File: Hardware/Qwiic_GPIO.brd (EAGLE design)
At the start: 38.1 x 38.1 mm, 74 parts, among them J2 SMD, J3 PTH, J4 SMD, J7 455-1750-1-ND, U3 TCA9534

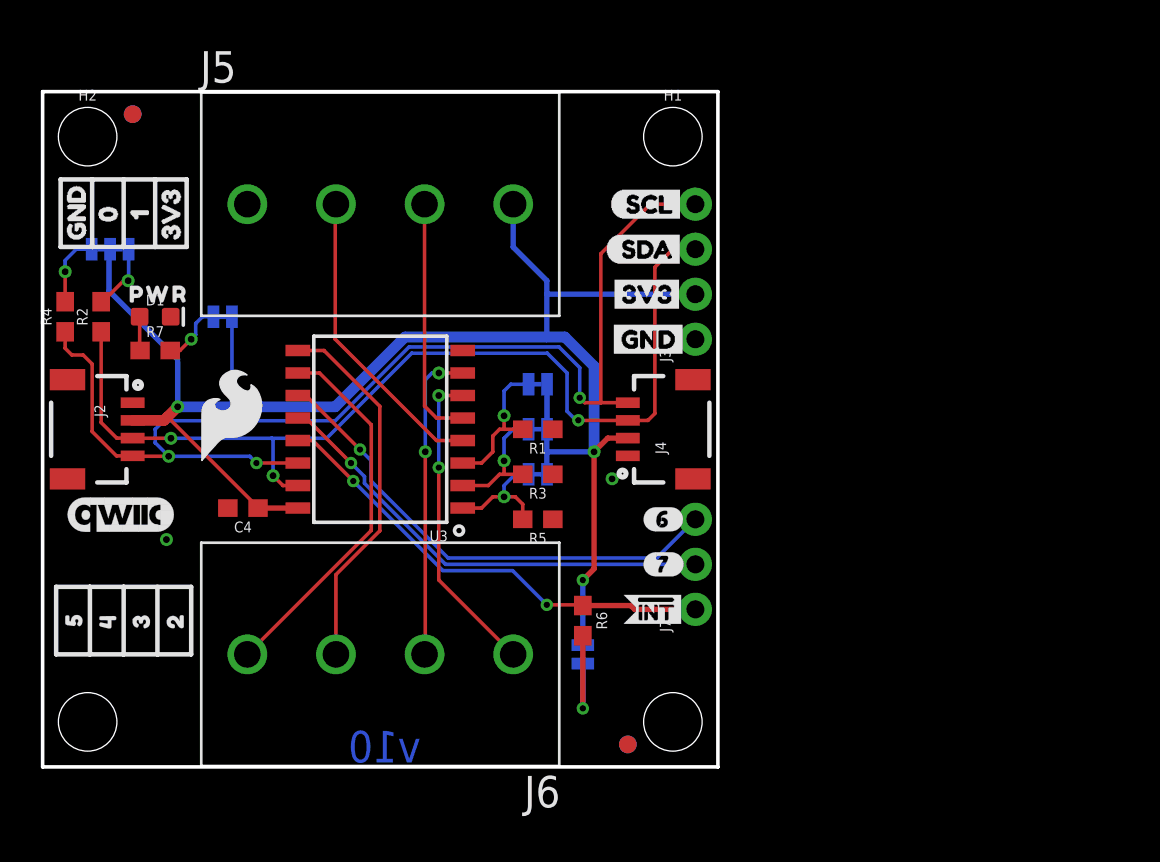
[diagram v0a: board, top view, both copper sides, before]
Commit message: adding rest of GPIO pins
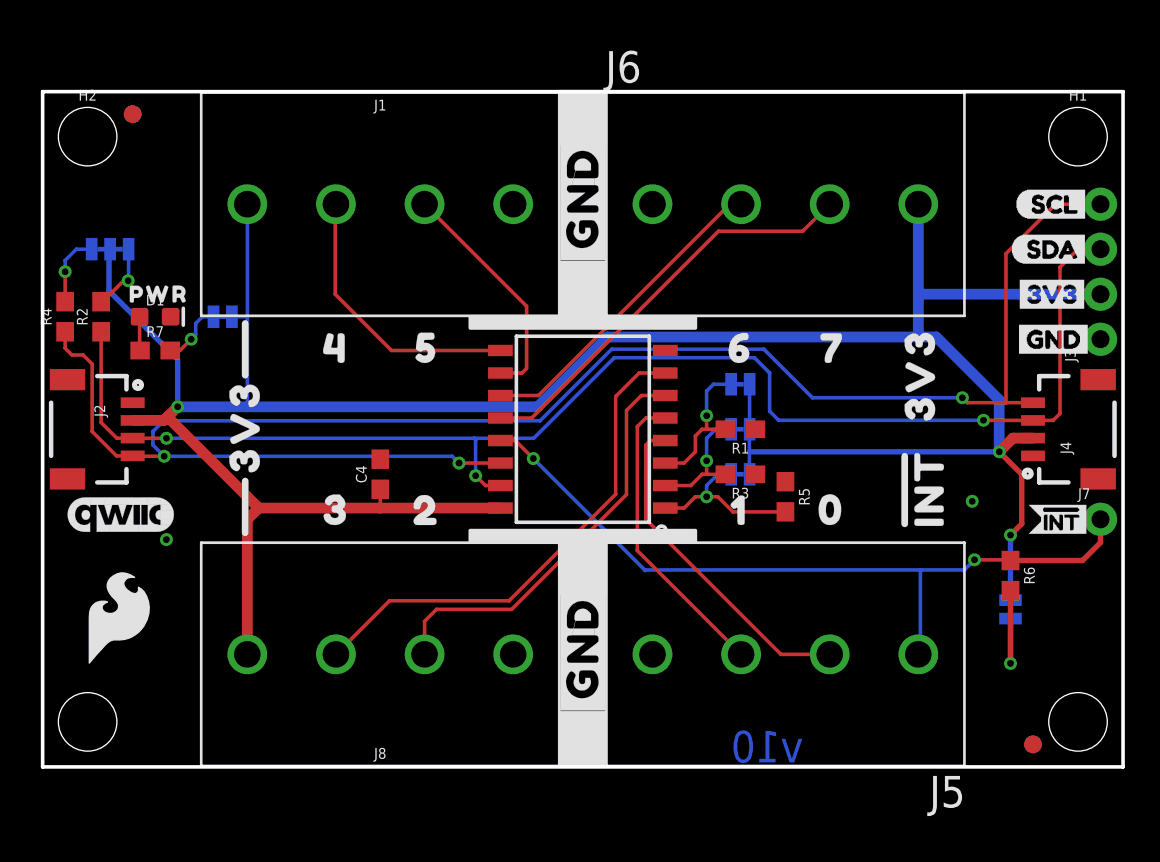
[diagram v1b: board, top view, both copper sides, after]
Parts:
- removed U$15: (no value), output:#_3_#0
- removed U$16: (no value), output:#_2_#0
- removed U$17: (no value), output:#_4_#0
- removed U$18: (no value), output:#_5_#0
- removed U$19: (no value), output:#_1_#0
- removed U$20: (no value), output:#_0_#0
- removed U$27: (no value), output:#GND#0
- removed U$28: (no value), output:#3V3#0
- added J1, J8: (no value), SparkFun-Connectors:LATCHTERMINAL-5MM-4
- added U$40: (no value), output:#GND#0
- J7: value 455-1750-1-ND -> (none); device SparkFun-Connectors:1X03_NO_SILK -> SparkFun-Connectors:1X01_NO_SILK
- U$14: device output:50 -> output:00
- U$29: device buzzard_labels (5):15 -> output:#INT0
- U$30, U$31: device output:#6#0 -> output:3V30
- U$32: device output:#7#0 -> output:40
- U$33: device output:#7#0 -> output:50
- U$35: device buzzard_labels (5):GND2 -> output:60
- U$37: device buzzard_labels (5):04 -> output:70
- U$38: device buzzard_labels (5):3V33 -> output:#GND#0
- U$4: device output:40 -> output:30
- U$6: device output:30 -> output:10
- moved LOGO2 62.1 mm to (10.2, -12.7)
- moved U$29 47.7 mm to (49.8, 12.3)
- moved FRAME1 42.2 mm to (-1.27, -10.2)
- moved U$14 41.4 mm to (42.5, 14.5), turned to 0 degrees
- moved U$37 39.5 mm to (42.7, 23.6), turned to 0 degrees
- moved U$35 35.9 mm to (37.5, 23.6), turned to 0 degrees
- moved U$38 35.1 mm to (30.5, 2.54)
- moved J5 34.2 mm to (41.9, 6.35), turned to 180 degrees
- moved J6 34.2 mm to (41.9, 31.8), turned to 0 degrees
- moved U$6 32.8 mm to (37.6, 14.5), turned to 0 degrees
- moved INT 24.3 mm to (54.6, 8.89)
- moved U$12 24.3 mm to (59.2, 8.89)
- moved R6 24.3 mm to (54.6, 10.8)
- moved J7 23.4 mm to (59.7, 14.0), turned to 0 degrees
- moved U$13 23.4 mm to (59.6, 14.0)
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- renumbered JP10 to I2C
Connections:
- net !INT: now also J5.1
- net 3.3V: now also J1.1, J6.4, J8.4; no longer J5.4
- net GND: now also J1.4, J5.4, J6.1, J8.1; no longer J5.1
- net P2: now also J8.2; no longer J6.1
- net P3: now also J8.3; no longer J6.2
- net P4: now also J1.2; no longer J6.3
- net P5: now also J1.3; no longer J6.4
- net P6: now also J6.2; no longer J7.3
- net P7: now also J6.3; no longer J7.2
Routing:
- net 3.3V: track 96.5 -> 156.9 mm
- net SCL: track 66.6 -> 99.8 mm
- net SDA: track 56.4 -> 79.1 mm
- net !INT: track 26.4 -> 43.8 mm
- net P3: track 17.8 -> 28.4 mm, vias 2 -> 0
- net P6: track 27.8 -> 18.1 mm, vias 1 -> 0
- net P5: track 21.2 -> 13.2 mm
- net P2: track 17.7 -> 23.5 mm, vias 2 -> 0
- net P4: track 20.9 -> 15.7 mm
- net P1: track 13.8 -> 17.1 mm
- net A0: track 6.96 -> 9.68 mm
- net P7: track 26.1 -> 23.6 mm, vias 1 -> 0
- net P0: track 17.2 -> 18.9 mm
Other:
- board size 38.1 x 38.1 mm -> 61 x 38.1 mm
- board text added: "Andy England"

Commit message: post checklist changes
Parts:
- removed J3: PTH, SparkX:1X04_NO_SILK
- removed U$36: (no value), output:#A0#0
- added J9: (no value), SparkFun-Connectors:1X04_NO_SILK
- added U$15: (no value), output:#ADR0#0
- J2, J4: value SMD -> QWIIC; device SparkX:1X04_1MM_RA -> SparkFun-Connectors:JST04_1MM_RA
- U$11: device output:#A2#0 -> output:#ADR2#0
- U$5: device output:#A1#0 -> output:#ADR1#0
- moved U$32 3.81 mm to (18.4, 23.6), turned to 180 degrees
- moved U$35 3.68 mm to (41.1, 23.6), turned to 180 degrees
- moved U$37 3.68 mm to (46.4, 23.6), turned to 180 degrees
- moved U$33 3.56 mm to (23.4, 23.6), turned to 180 degrees
- moved C4 3.11 mm to (22.1, 17.1)
- moved U$5 2.03 mm to (45.5, 19.1)
- moved U$11 2.03 mm to (45.7, 21.6)
- renumbered 3V3 to PWR, A0 to ADR0, A1 to ADR1, A2 to ADR2
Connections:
- net A0 renamed ADR0
- net A1 renamed ADR1
- net A2 renamed ADR2
- net 3.3V: now also J9.2; no longer J3.2
- net GND: now also J9.1; no longer J3.1
- net SCL: now also J9.4; no longer J3.4
- net SDA: now also J9.3; no longer J3.3
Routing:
- net P3: track 28.4 -> 27.6 mm
- net 3.3V: track 156.9 -> 157.5 mm

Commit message: uploading panel
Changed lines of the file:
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@@
 <layer number="24" name="bOrigins" color="15" fill="1" visible="yes" active="yes"/>
 <layer number="25" name="tNames" color="7" fill="1" visible="yes" active="yes"/>
-<layer number="26" name="bNames" color="7" fill="1" visible="no" active="yes"/>
-<layer number="27" name="tValues" color="7" fill="1" visible="no" active="yes"/>
-<layer number="28" name="bValues" color="7" fill="1" visible="no" active="yes"/>
-<layer number="29" name="tStop" color="7" fill="3" visible="no" active="yes"/>
-<layer number="30" name="bStop" color="7" fill="6" visible="no" active="yes"/>
-<layer number="31" name="tCream" color="7" fill="4" visible="no" active="yes"/>
-<layer number="32" name="bCream" color="7" fill="5" visible="no" active="yes"/>
-<layer number="33" name="tFinish" color="6" fill="3" visible="no" active="yes"/>
-<layer number="34" name="bFinish" color="6" fill="6" visible="no" active="yes"/>
-<layer number="35" name="tGlue" color="7" fill="4" visible="no" active="yes"/>
-<layer number="36" name="bGlue" color="7" fill="5" visible="no" active="yes"/>
-<layer number="37" name="tTest" color="7" fill="1" visible="no" active="yes"/>
-<layer number="38" name="bTest" color="7" fill="1" visible="no" active="yes"/>
+<layer number="26" name="bNames" color="7" fill="1" visible="yes" active="yes"/>
+<layer number="27" name="tValues" color="7" fill="1" visible="yes" active="yes"/>
+<layer number="28" name="bValues" color="7" fill="1" visible="yes" active="yes"/>
+<layer number="29" name="tStop" color="7" fill="3" visible="yes" active="yes"/>
+<layer number="30" name="bStop" color="7" fill="6" visible="yes" active="yes"/>
+<layer number="31" name="tCream" color="7" fill="4" visible="yes" active="yes"/>
+<layer number="32" name="bCream" color="7" fill="5" visible="yes" active="yes"/>
+<layer number="33" name="tFinish" color="6" fill="3" visible="yes" active="yes"/>
+<layer number="34" name="bFinish" color="6" fill="6" visible="yes" active="yes"/>
+<layer number="35" name="tGlue" color="7" fill="4" visible="yes" active="yes"/>
+<layer number="36" name="bGlue" color="7" fill="5" visible="yes" active="yes"/>
+<layer number="37" name="tTest" color="7" fill="1" visible="yes" active="yes"/>
+<layer number="38" name="bTest" color="7" fill="1" visible="yes" active="yes"/>
 <layer number="39" name="tKeepout" color="4" fill="11" visible="yes" active="yes"/>
 <layer number="40" name="bKeepout" color="1" fill="11" visible="yes" active="yes"/>
@@
 <wire x1="11.55" y1="13.963" x2="12.192" y2="14.605" width="0.6096" layer="1"/>
 <wire x1="11.55" y1="31.75" x2="11.557" y2="31.743" width="0.2032" layer="16"/>
-<wire x1="11.557" y1="31.743" x2="11.557" y2="25.4" width="0.2032" layer="16"/>
+<wire x1="11.557" y1="31.743" x2="11.557" y2="25.4" width="0.6096" layer="16"/>
 <wire x1="49.41" y1="31.75" x2="49.41" y2="26.67" width="0.6096" layer="16"/>
 <wire x1="49.41" y1="26.67" x2="49.41" y2="24.264" width="0.6096" layer="16"/>
 <wire x1="49.41" y1="24.264" x2="49.403" y2="24.257" width="0.2032" layer="16"/>
-<wire x1="11.557" y1="25.4" x2="11.557" y2="20.32" width="0.2032" layer="16"/>
+<wire x1="11.557" y1="25.4" x2="11.557" y2="20.32" width="0.6096" layer="16"/>
 <wire x1="39.8907" y1="19.05" x2="39.878" y2="19.0373" width="0.2032" layer="16"/>
 <contactref element="J9" pad="2"/>
